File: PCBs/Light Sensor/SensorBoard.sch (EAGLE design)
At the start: 21 parts, among them J1 AVR_SPI_PRG_6PTH

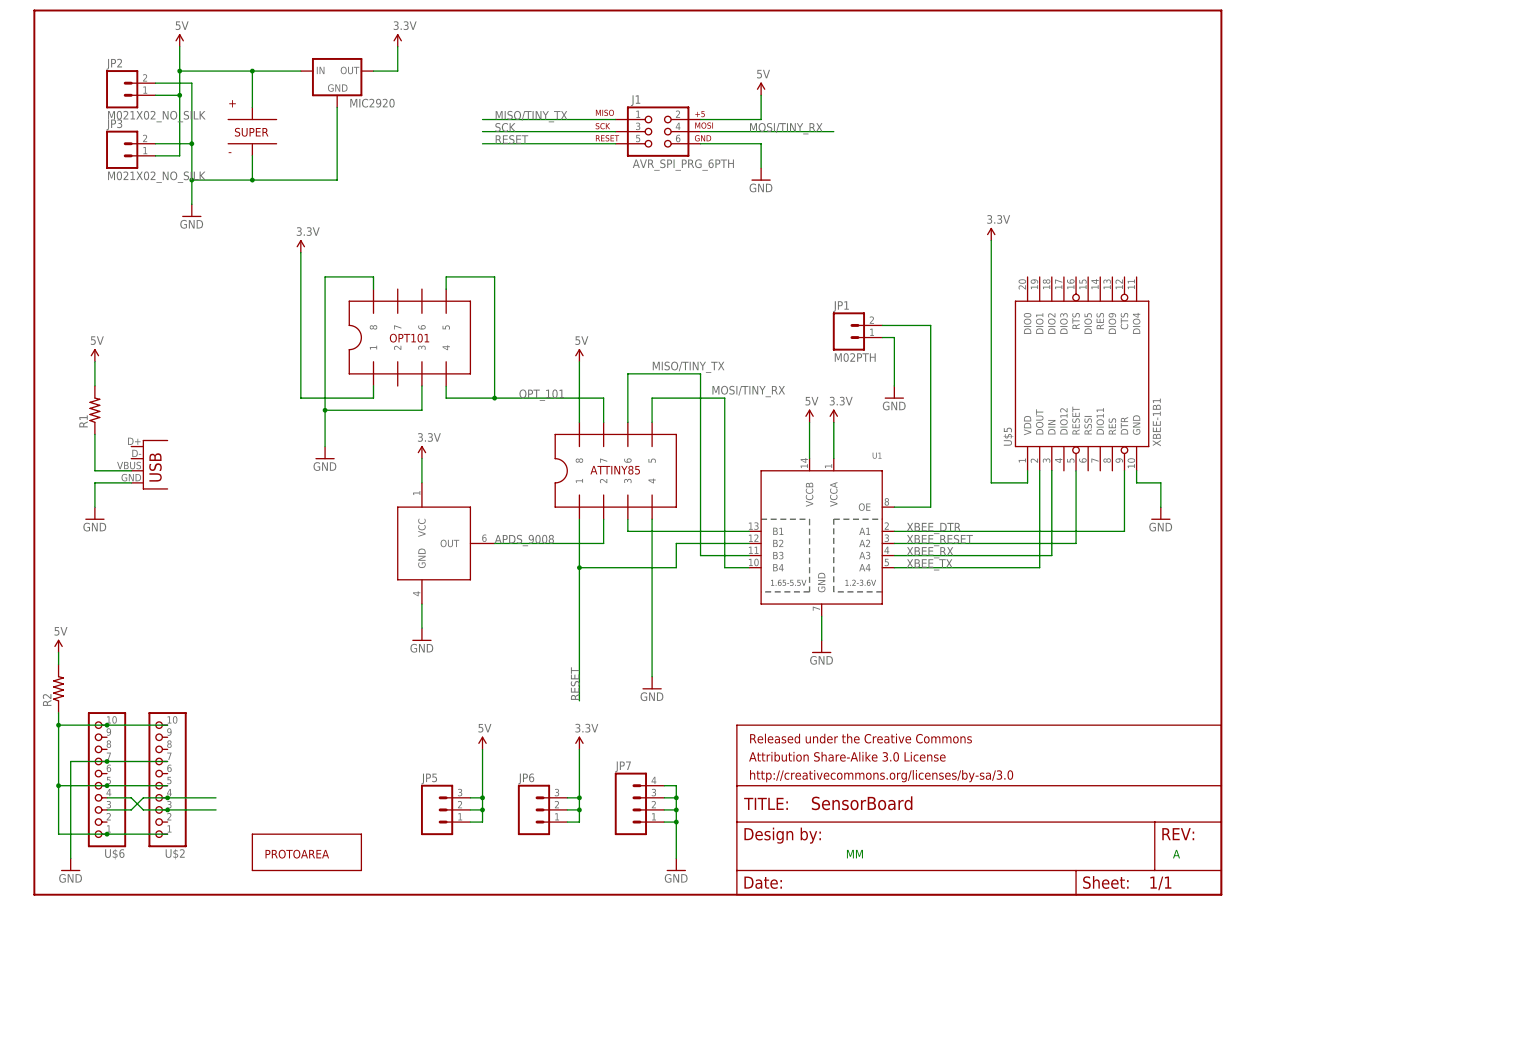
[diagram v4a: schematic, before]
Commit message: Added caps, back to DIPs on everything, fixups, screw holes
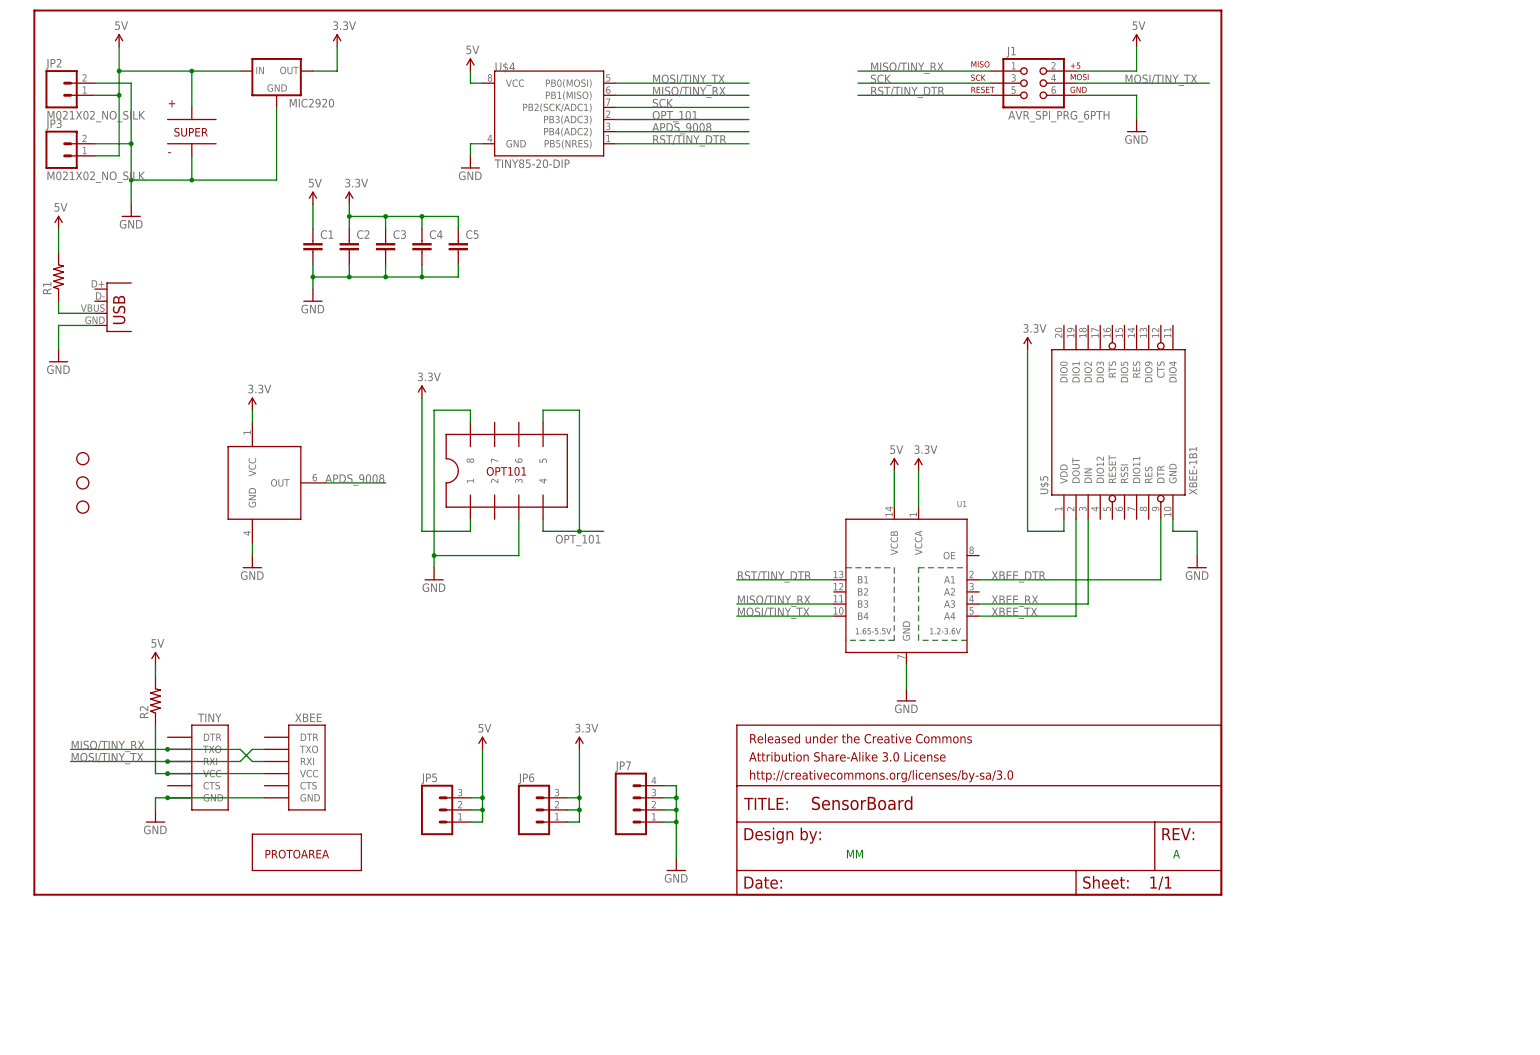
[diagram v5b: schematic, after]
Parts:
- removed JP1: M02PTH, SparkFun-Connectors:M02PTH
- removed U$2, U$6: PINHD-1X10, adafruit:PINHD-1X10
- added C1, C2, C3, C4, C5: (no value), SparkFun-Capacitors:CAP1210
- added STANDOFF1, STANDOFF2, STANDOFF3: STAND-OFF, SparkFun-Electromechanical:STAND-OFF
- added TINY, XBEE: FTDI_DEVICE, SparkFun-Connectors:FTDI_DEVICE
- U$1: value OPT101SMD -> OPT101TH; device MyLibrary:OPT101SMD -> MyLibrary:OPT101TH
- U$4: value ATTINY85SMD -> TINY85-20-DIP; device MyLibrary:ATTINY85SMD -> SparkFun-DigitalIC:ATTINY45TINY85-20-DIP
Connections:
- removed net MISO/TINY_TX: J1.1, U$4.6, U1.B3
- removed net MOSI/TINY_RX: J1.4, U$4.5, U1.B4
- removed net N$3: U$2.4, U$6.3
- removed net N$4: R2.1, U$2.1, U$2.10, U$2.5, U$6.1, U$6.10, U$6.5
- removed net N$5: JP1.2, U1.OE
- removed net RESET: J1.5, U$4.1, U1.B2
- removed net TINY_DTR: U$4.3, U1.B1
- removed net XBEE_RESET: U$5.RESET, U1.A2
- new net MISO/TINY_RX: J1.1, TINY.TXO, U$4.PB1(MISO), U1.B3, XBEE.RXI
- new net MOSI/TINY_TX: J1.4, TINY.RXI, U$4.PB0(MOSI), U1.B4, XBEE.TXO
- new net RST/TINY_DTR: J1.5, U$4.PB5(NRES), U1.B1
- net 3.3V: now also C2.1, C3.1, C4.1, C5.1
- net 5V: now also C1.1, U$4.VCC; no longer U$4.8
- net APDS_9008: now also U$4.PB4(ADC2); no longer U$4.2
- net GND: now also C1.2, C2.2, C3.2, C4.2, C5.2, TINY.GND, U$4.GND, XBEE.GND; no longer JP1.1, U$2.7, U$4.4, U$6.7
- net N$2: now also R2.1, TINY.VCC, XBEE.VCC; no longer U$2.3, U$6.4
- net OPT_101: now also U$4.PB3(ADC3); no longer U$4.7
- net SCK: now also U$4.PB2(SCK/ADC1)
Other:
- moved on the sheet: J1, JP2, JP3, MIC2920, R1, R2, U$5, U1

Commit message: Version taped out for rev A
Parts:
- added JP1: M021X02_NO_SILK, SparkFun-Connectors:M021X02_NO_SILK
- U1: device SparkFun-DigitalIC:TXB0104PWRSOIC14 -> MyLibrary:TXB0104PWRSOIC14
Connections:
- net GND: now also JP1.2
- net N$1: now also JP1.1
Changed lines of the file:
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@@
 <grid distance="0.1" unitdist="inch" unit="inch" style="lines" multiple="1" display="no" altdistance="0.01" altunitdist="inch" altunit="inch"/>
 <layers>
-<layer number="1" name="Top" color="4" fill="1" visible="yes" active="no"/>
-<layer number="2" name="Route2" color="1" fill="3" visible="yes" active="no"/>
-<layer number="3" name="Route3" color="4" fill="3" visible="yes" active="no"/>
-<layer number="14" name="Route14" color="1" fill="6" visible="yes" active="no"/>
-<layer number="15" name="Route15" color="4" fill="6" visible="yes" active="no"/>
-<layer number="16" name="Bottom" color="1" fill="1" visible="yes" active="no"/>
-<layer number="17" name="Pads" color="2" fill="1" visible="yes" active="no"/>
-<layer number="18" name="Vias" color="2" fill="1" visible="yes" active="no"/>
-<layer number="19" name="Unrouted" color="6" fill="1" visible="yes" active="no"/>
-<layer number="20" name="Dimension" color="15" fill="1" visible="yes" active="no"/>
-<layer number="21" name="tPlace" color="7" fill="1" visible="yes" active="no"/>
-<layer number="22" name="bPlace" color="7" fill="1" visible="yes" active="no"/>
-<layer number="23" name="tOrigins" color="15" fill="1" visible="yes" active="no"/>
-<layer number="24" name="bOrigins" color="15" fill="1" visible="yes" active="no"/>
-<layer number="25" name="tNames" color="7" fill="1" visible="yes" active="no"/>
-<layer number="26" name="bNames" color="7" fill="1" visible="yes" active="no"/>
-<layer number="27" name="tValues" color="7" fill="1" visible="yes" active="no"/>
-<layer number="28" name="bValues" color="7" fill="1" visible="yes" active="no"/>
+<layer number="1" name="Top" color="4" fill="1" visible="no" active="no"/>
+<layer number="2" name="Route2" color="1" fill="3" visible="no" active="no"/>
+<layer number="3" name="Route3" color="4" fill="3" visible="no" active="no"/>
+<layer number="14" name="Route14" color="1" fill="6" visible="no" active="no"/>
+<layer number="15" name="Route15" color="4" fill="6" visible="no" active="no"/>
+<layer number="16" name="Bottom" color="1" fill="1" visible="no" active="no"/>
+<layer number="17" name="Pads" color="2" fill="1" visible="no" active="no"/>
+<layer number="18" name="Vias" color="2" fill="1" visible="no" active="no"/>
+<layer number="19" name="Unrouted" color="6" fill="1" visible="no" active="no"/>
+<layer number="20" name="Dimension" color="15" fill="1" visible="no" active="no"/>
+<layer number="21" name="tPlace" color="7" fill="1" visible="no" active="no"/>
+<layer number="22" name="bPlace" color="7" fill="1" visible="no" active="no"/>
+<layer number="23" name="tOrigins" color="15" fill="1" visible="no" active="no"/>
+<layer number="24" name="bOrigins" color="15" fill="1" visible="no" active="no"/>
+<layer number="25" name="tNames" color="7" fill="1" visible="no" active="no"/>
+<layer number="26" name="bNames" color="7" fill="1" visible="no" active="no"/>
+<layer number="27" name="tValues" color="7" fill="1" visible="no" active="no"/>
+<layer number="28" name="bValues" color="7" fill="1" visible="no" active="no"/>
 <layer number="29" name="tStop" color="7" fill="3" visible="no" active="no"/>
 <layer number="30" name="bStop" color="7" fill="6" visible="no" active="no"/>
@@
 <layer number="35" name="tGlue" color="7" fill="4" visible="no" active="no"/>
 <layer number="36" name="bGlue" color="7" fill="5" visible="no" active="no"/>
-<layer number="37" name="tTest" color="7" fill="1" visible="yes" active="no"/>
-<layer number="38" name="bTest" color="7" fill="1" visible="yes" active="no"/>
+<layer number="37" name="tTest" color="7" fill="1" visible="no" active="no"/>
+<layer number="38" name="bTest" color="7" fill="1" visible="no" active="no"/>
 <layer number="39" name="tKeepout" color="4" fill="11" visible="no" active="no"/>
 <layer number="40" name="bKeepout" color="1" fill="11" visible="no" active="no"/>
@@
 <layer number="44" name="Drills" color="7" fill="1" visible="no" active="no"/>
 <layer number="45" name="Holes" color="7" fill="1" visible="no" active="no"/>
-<layer number="46" name="Milling" color="3" fill="1" visible="yes" active="no"/>
-<layer number="47" name="Measures" color="7" fill="1" visible="yes" active="no"/>
-<layer number="48" name="Document" color="7" fill="1" visible="yes" active="no"/>
-<layer number="49" name="Reference" color="7" fill="1" visible="yes" active="no"/>
-<layer number="50" name="dxf" color="7" fill="1" visible="yes" active="no"/>
-<layer number="51" name="tDocu" color="7" fill="1" visible="yes" active="no"/>
-<layer number="52" name="bDocu" color="7" fill="1" visible="yes" active="no"/>
-<layer number="53" name="tGND_GNDA" color="7" fill="9" visible="yes" active="no"/>
-<layer number="54" name="bGND_GNDA" color="1" fill="9" visible="yes" active="no"/>
-<layer number="56" name="wert" color="7" fill="1" visible="yes" active="no"/>
-<layer number="57" name="tCAD" color="7" fill="1" visible="yes" active="no"/>
+<layer number="46" name="Milling" color="3" fill="1" visible="no" active="no"/>
+<layer number="47" name="Measures" color="7" fill="1" visible="no" active="no"/>
+<layer number="48" name="Document" color="7" fill="1" visible="no" active="no"/>
+<layer number="49" name="Reference" color="7" fill="1" visible="no" active="no"/>
+<layer number="50" name="dxf" color="7" fill="1" visible="no" active="no"/>
+<layer number="51" name="tDocu" color="7" fill="1" visible="no" active="no"/>
+<layer number="52" name="bDocu" color="7" fill="1" visible="no" active="no"/>
+<layer number="53" name="tGND_GNDA" color="7" fill="9" visible="no" active="no"/>
+<layer number="54" name="bGND_GNDA" color="1" fill="9" visible="no" active="no"/>
+<layer number="56" name="wert" color="7" fill="1" visible="no" active="no"/>
+<layer number="57" name="tCAD" color="7" fill="1" visible="no" active="no"/>
 <layer number="90" name="Modules" color="5" fill="1" visible="yes" active="yes"/>
 <layer number="91" name="Nets" color="2" fill="1" visible="yes" active="yes"/>
@@
 <part name="GND4" library="supply1" deviceset="GND" device=""/>
 <part name="GND5" library="supply1" deviceset="GND" device=""/>
-<part name="U1" library="SparkFun-DigitalIC" deviceset="TXB0104PWR" device="SOIC14"/>
+<part name="U1" library="MyLibrary" deviceset="TXB0104PWR" device="SOIC14"/>
 <part name="SUPPLY5" library="SparkFun-Aesthetics" deviceset="5V" device=""/>
 <part name="SUPPLY8" library="SparkFun-Aesthetics" deviceset="3.3V" device=""/>
@@
 <part name="STANDOFF3" library="SparkFun-Electromechanical" deviceset="STAND-OFF" device=""/>
 <part name="C5" library="SparkFun-Capacitors" deviceset="CAP" device="1210"/>
+<part name="JP1" library="SparkFun-Connectors" deviceset="M02" device="1X02_NO_SILK"/>
 </parts>
 <sheets>
@@
 <instance part="JP4" gate="G$1" x="15.24" y="119.38"/>
 <instance part="R1" gate="G$1" x="5.08" y="129.54" rot="R90"/>
-<instance part="GND10" gate="1" x="5.08" y="111.76"/>
+<instance part="GND10" gate="1" x="5.08" y="88.9"/>
 <instance part="FRAME1" gate="G$1" x="0" y="0"/>
 <instance part="FRAME1" gate="G$2" x="147.32" y="0"/>
@@
 <instance part="SUPPLY15" gate="G$1" x="66.04" y="144.78"/>
 <instance part="GND12" gate="1" x="58.42" y="124.46"/>
-<instance part="STANDOFF1" gate="G$1" x="10.16" y="91.44"/>
-<instance part="STANDOFF2" gate="G$1" x="10.16" y="86.36"/>
-<instance part="STANDOFF3" gate="G$1" x="10.16" y="81.28"/>
+<instance part="STANDOFF1" gate="G$1" x="5.08" y="66.04"/>
+<instance part="STANDOFF2" gate="G$1" x="5.08" y="60.96"/>
+<instance part="STANDOFF3" gate="G$1" x="5.08" y="55.88"/>
 <instance part="C5" gate="G$1" x="88.9" y="134.62"/>
+<instance part="JP1" gate="G$1" x="20.32" y="101.6" rot="R180"/>
 </instances>
 <busses>
@@
 <pinref part="GND10" gate="1" pin="GND"/>
 <wire x1="12.7" y1="119.38" x2="5.08" y2="119.38" width="0.1524" layer="91"/>
-<wire x1="5.08" y1="119.38" x2="5.08" y2="114.3" width="0.1524" layer="91"/>
+<wire x1="5.08" y1="119.38" x2="5.08" y2="99.06" width="0.1524" layer="91"/>
+<pinref part="JP1" gate="G$1" pin="2"/>
+<wire x1="5.08" y1="99.06" x2="5.08" y2="91.44" width="0.1524" layer="91"/>
+<wire x1="12.7" y1="99.06" x2="5.08" y2="99.06" width="0.1524" layer="91"/>
+<junction x="5.08" y="99.06"/>
 </segment>
 <segment>
@@
 <pinref part="JP4" gate="G$1" pin="VBUS"/>
 <pinref part="R1" gate="G$1" pin="1"/>
-<wire x1="12.7" y1="121.92" x2="5.08" y2="121.92" width="0.1524" layer="91"/>
+<wire x1="12.7" y1="121.92" x2="7.62" y2="121.92" width="0.1524" layer="91"/>
+<wire x1="7.62" y1="121.92" x2="5.08" y2="121.92" width="0.1524" layer="91"/>
 <wire x1="5.08" y1="121.92" x2="5.08" y2="124.46" width="0.1524" layer="91"/>
-</segment>
-</net>
+<wire x1="7.62" y1="121.92" x2="7.62" y2="101.6" width="0.1524" layer="91"/>
+<junction x="7.62" y="121.92"/>
+<pinref part="JP1" gate="G$1" pin="1"/>
+<wire x1="7.62" y1="101.6" x2="12.7" y2="101.6" width="0.1524" layer="91"/>
+</segment>
+</net>
